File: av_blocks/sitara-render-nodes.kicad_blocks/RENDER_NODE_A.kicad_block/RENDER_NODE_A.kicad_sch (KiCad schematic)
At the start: 4 parts

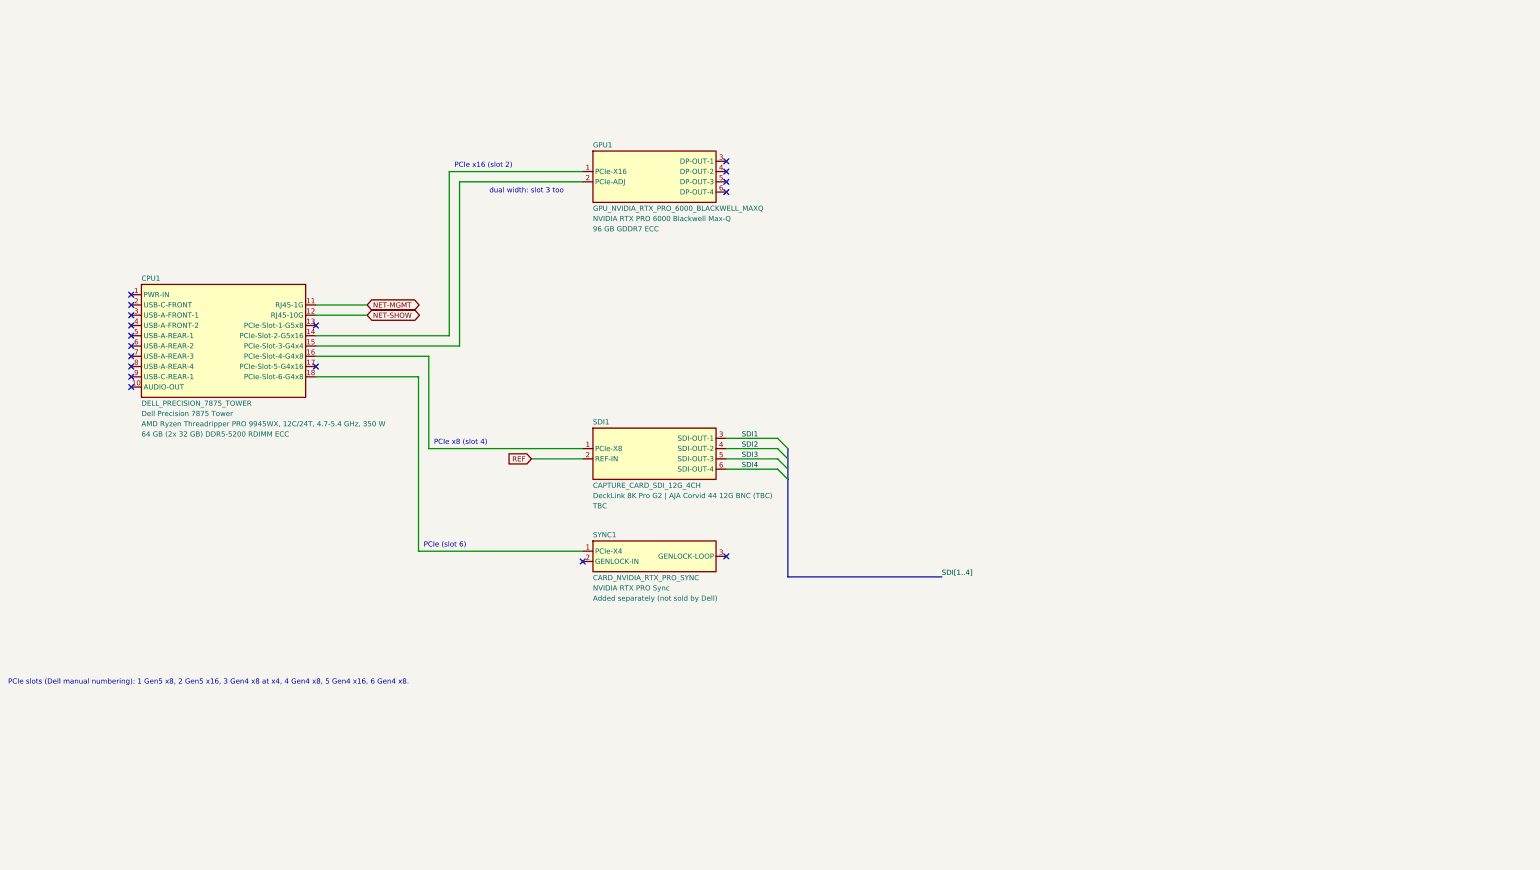
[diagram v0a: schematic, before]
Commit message: Add sitara_av generator package, project scaffolder and template, design blocks, print variant, CI and leak scan; migrate legacy pin names; add generic AV symbols and sitara-audio library
Co-Authored-By: Claude Sonnet 5.5 <noreply@anthropic.com>
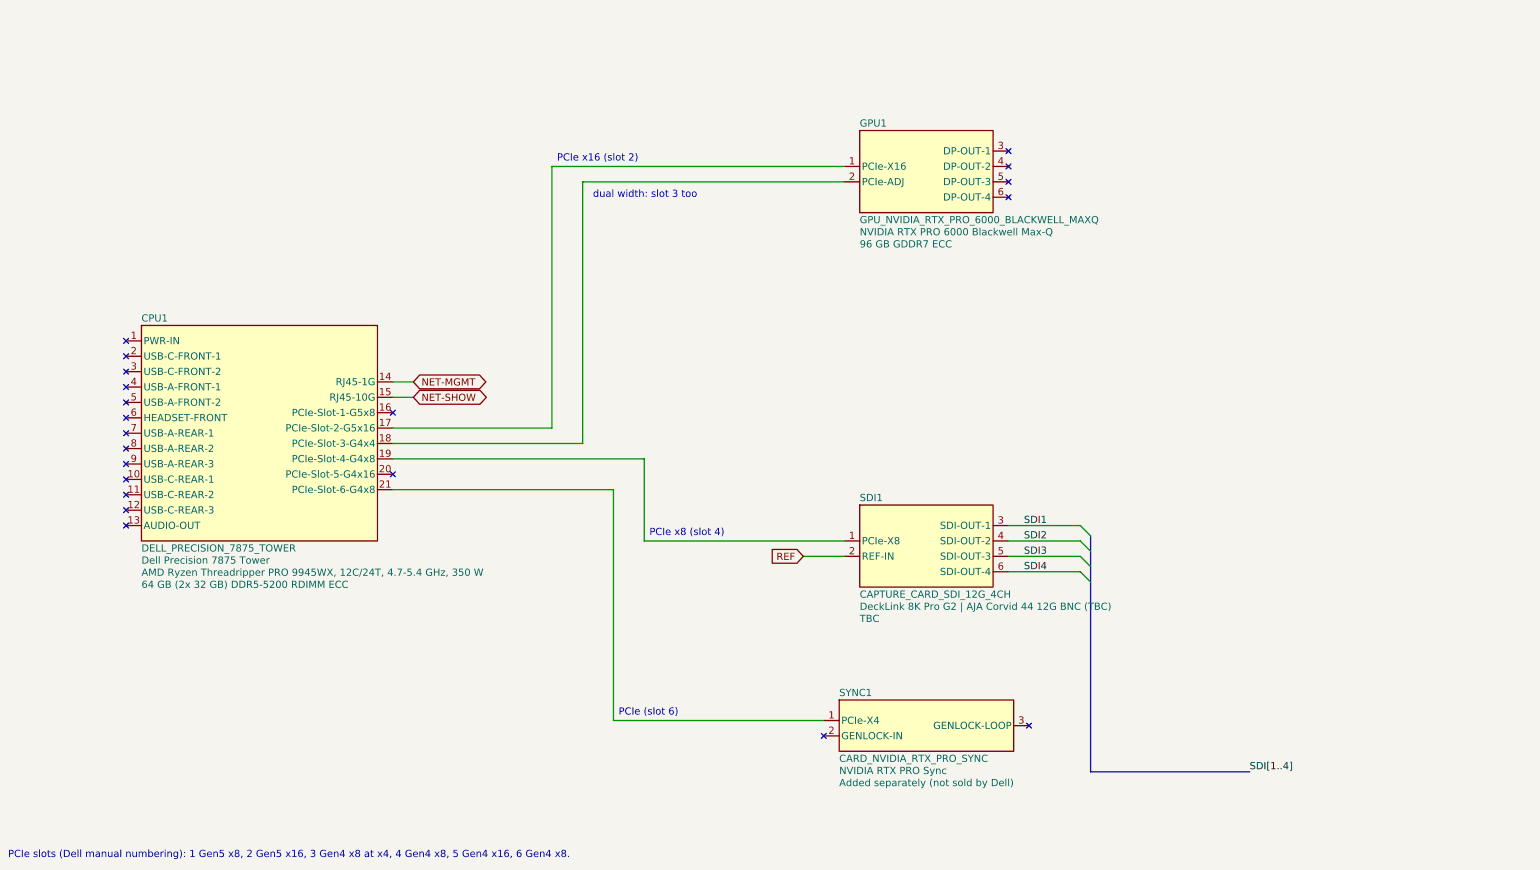
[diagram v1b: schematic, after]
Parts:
- CPU1: Ethernet RJ45 1 GbE (Realtek RTL8111-EPP) + RJ45 10 GbE (Marvell AQC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 -> (none); Management AMD DASH per Dell product page; which port carries it TBC -> AMD DASH; which port carries it TBC; Network Integrated: 1x RJ45 1 GbE + 1x RJ45 10 GbE (Dell spec page) -> Integrated: RJ45 1 GbE (Realtek RTL8111-EPP) + RJ45 10 GbE 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
- GPU1: DisplayOutputs 4x DisplayPort (DP 2.1 per NVIDIA - verify) -> 4x DisplayPort 2.1
- SYNC1: Status CONFIRMED -> TBC
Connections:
- net NET-MGMT: now also CPU1.14 (RJ45-1G); no longer CPU1.11 (RJ45-1G)
- net NET-SHOW: now also CPU1.15 (RJ45-10G); no longer CPU1.12 (RJ45-10G)
- net at CPU1.16 (PCIe-Slot-1-G5x8): no longer SDI1.1 (PCIe-X8)
- net at CPU1.18 (PCIe-Slot-3-G4x4): now also GPU1.2 (PCIe-ADJ); no longer SYNC1.1 (PCIe-X4)
- net at GPU1.1 (PCIe-X16): now also CPU1.17 (PCIe-Slot-2-G5x16); no longer CPU1.14 (PCIe-Slot-2-G5x16)
- new net: CPU1.19 (PCIe-Slot-4-G4x8), SDI1.1 (PCIe-X8)
- new net: CPU1.21 (PCIe-Slot-6-G4x8), SYNC1.1 (PCIe-X4)
- no-connect marks 18 -> 21
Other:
- title: Render node A (design block) -> Render Node A (design block)

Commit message: Add TBC register (sitara_av.tbc, av-tbc-register skill, scaffold and template page); larger note text; update Dell, Sync card and Protectli fields
Co-Authored-By: Claude Sonnet 5.5 <noreply@anthropic.com>
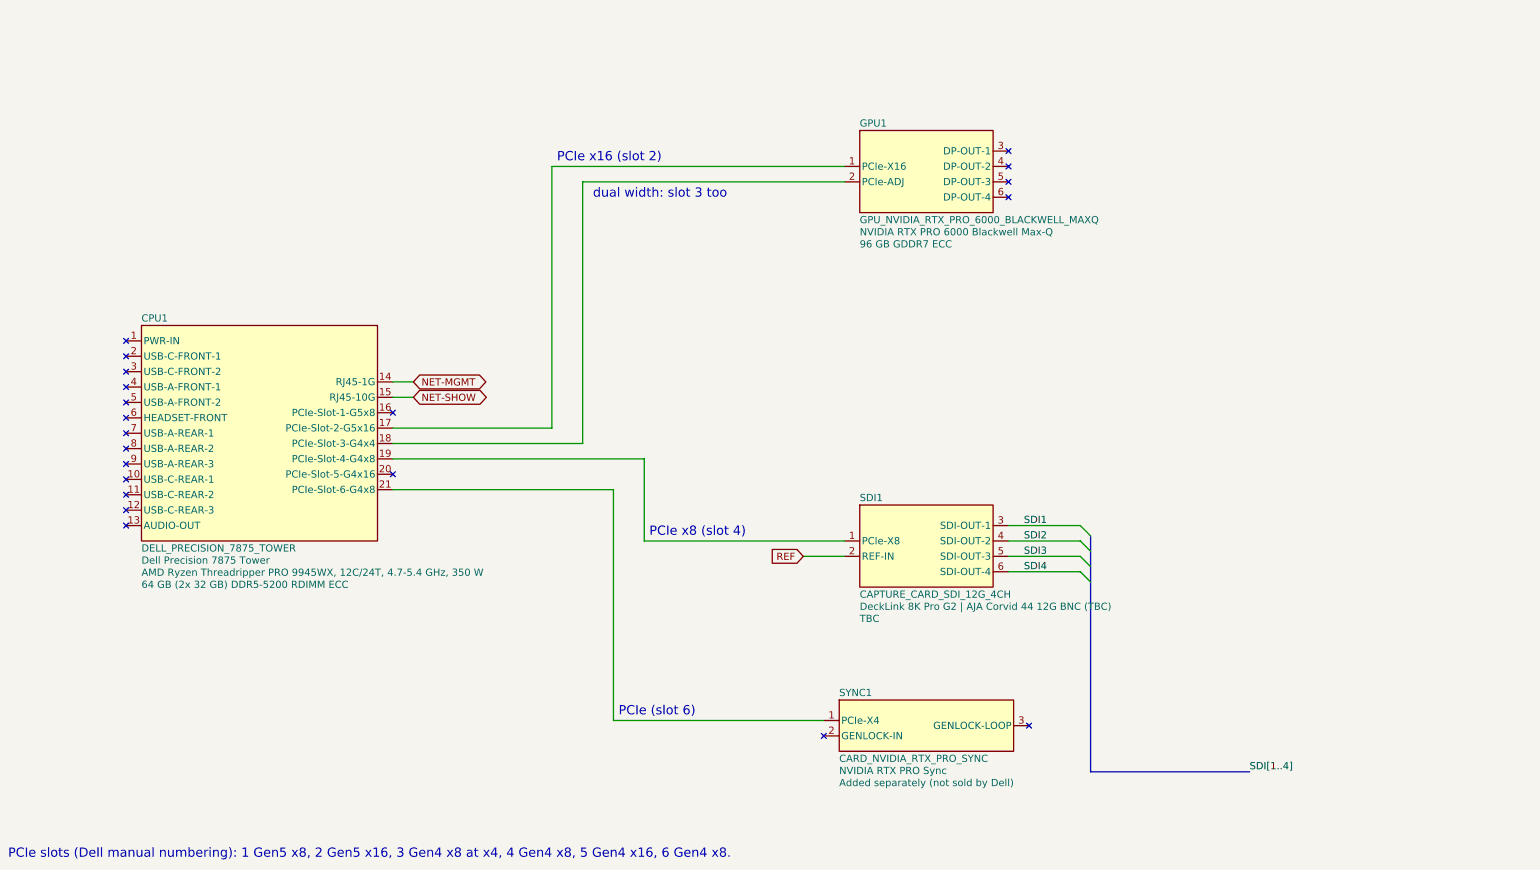
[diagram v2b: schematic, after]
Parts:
- CPU1: Management AMD DASH; which port carries it TBC -> AMD DASH; suspected on the 1 GbE jack, to be confirmed when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; Mounting (none) -> Dell rail kit 3WF88 / 03W88, 4U
- SYNC1: Lanes x4 assumed (TBC) -> Drawn as x4 for slot accounting. Reportedly uses no PCIe da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; SlotWidth 1 (assumed, TBC) -> 1 (retailer listing; vendor datasheet not found)
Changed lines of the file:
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@@
 		(effects
 			(font
-				(size 1.78 1.78)
+				(size 2.29 2.29)
 			)
 			(justify left bottom)
@@
 		(effects
 			(font
-				(size 1.78 1.78)
+				(size 2.29 2.29)
 			)
 			(justify left bottom)
@@
 		(effects
 			(font
-				(size 1.78 1.78)
+				(size 2.29 2.29)
 			)
 			(justify left bottom)
@@
 		(effects
 			(font
-				(size 1.78 1.78)
+				(size 2.29 2.29)
 			)
 			(justify left bottom)
@@
 		(effects
 			(font
-				(size 1.78 1.78)
+				(size 2.29 2.29)
 			)
 			(justify left bottom)
@@
 			)
 		)
-		(property "Management" "AMD DASH; which port carries it TBC"
+		(property "Management" "AMD DASH; suspected on the 1 GbE jack, to be confirmed when the unit arrives (Oct 28)"
 			(at 85.09 134.62 0)
 			(hide yes)
@@
 		)
 		(property "FormFactor" "Tower Workstation"
+			(at 85.09 134.62 0)
+			(hide yes)
+			(show_name no)
+			(do_not_autoplace no)
+			(effects
+				(font
+					(size 1.78 1.78)
+				)
+			)
+		)
+		(property "Mounting" "Dell rail kit 3WF88 / 03W88, 4U"
 			(at 85.09 134.62 0)
 			(hide yes)
@@
 			)
 		)
-		(property "SlotWidth" "1 (assumed, TBC)"
+		(property "SlotWidth" "1 (retailer listing; vendor datasheet not found)"
 			(at 250.19 207.01 0)
 			(hide yes)
@@
 			)
 		)
-		(property "Lanes" "x4 assumed (TBC)"
+		(property "Lanes" "Drawn as x4 for slot accounting. Reportedly uses no PCIe data lines (sync runs over ribbon cables to each GPU), electrical lanes not published"
 			(at 250.19 207.01 0)
 			(hide yes)

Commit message: Add power budget helper and PowerW symbol fields; record Dell 7875 C20 inlet and 1350 W maximum
Co-Authored-By: Claude Sonnet 5.5 <noreply@anthropic.com>
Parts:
- CPU1: PSU 1350 W -> 1350 W Platinum, C20 inlet (owner's manual); 90-264 VAC, 16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; PowerBasis (none) -> Dell PSU rating: maximum for the whole node, installed card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; PowerTypicalBasis (none) -> estimate: CPU 350 W + GPU 300 W + about 150 W other; PowerTypicalW (none) -> 800; PowerW (none) -> 1350
- GPU1: PowerBasis (none) -> NVIDIA spec (Max-Q); PowerDraw 300 W -> (none); PowerIncludedIn (none) -> host; PowerW (none) -> 300
- SDI1, SYNC1: PowerIncludedIn (none) -> host
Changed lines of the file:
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@@
 			)
 		)
-		(property "PSU" "1350 W"
+		(property "PSU" "1350 W Platinum, C20 inlet (owner's manual); 90-264 VAC, 16 A max"
+			(at 85.09 134.62 0)
+			(hide yes)
+			(show_name no)
+			(do_not_autoplace no)
+			(effects
+				(font
+					(size 1.78 1.78)
+				)
+			)
+		)
+		(property "PowerW" "1350"
+			(at 85.09 134.62 0)
+			(hide yes)
+			(show_name no)
+			(do_not_autoplace no)
+			(effects
+				(font
+					(size 1.78 1.78)
+				)
+			)
+		)
+		(property "PowerBasis" "Dell PSU rating: maximum for the whole node, installed cards included"
+			(at 85.09 134.62 0)
+			(hide yes)
+			(show_name no)
+			(do_not_autoplace no)
+			(effects
+				(font
+					(size 1.78 1.78)
+				)
+			)
+		)
+		(property "PowerTypicalW" "800"
+			(at 85.09 134.62 0)
+			(hide yes)
+			(show_name no)
+			(do_not_autoplace no)
+			(effects
+				(font
+					(size 1.78 1.78)
+				)
+			)
+		)
+		(property "PowerTypicalBasis" "estimate: CPU 350 W + GPU 300 W + about 150 W other"
 			(at 85.09 134.62 0)
 			(hide yes)
@@
 			)
 		)
+		(property "PowerIncludedIn" "host"
+			(at 250.19 207.01 0)
+			(hide yes)
+			(show_name no)
+			(do_not_autoplace no)
+			(effects
+				(font
+					(size 1.78 1.78)
+				)
+			)
+		)
 		(property "Model" "NVIDIA RTX PRO Sync"
 			(at 228.6 217.12 0)
@@
 			)
 		)
-		(property "PowerDraw" "300 W"
+		(property "PowerW" "300"
+			(at 250.19 69.85 0)
+			(hide yes)
+			(show_name no)
+			(do_not_autoplace no)
+			(effects
+				(font
+					(size 1.78 1.78)
+				)
+			)
+		)
+		(property "PowerBasis" "NVIDIA spec (Max-Q)"
+			(at 250.19 69.85 0)
+			(hide yes)
+			(show_name no)
+			(do_not_autoplace no)
+			(effects
+				(font
+					(size 1.78 1.78)
+				)
+			)
+		)
+		(property "PowerIncludedIn" "host"
 			(at 250.19 69.85 0)
 			(hide yes)
@@
 			(at 250.19 162.56 0)
 			(hide yes)
+			(show_name no)
+			(do_not_autoplace no)
+			(effects
+				(font
+					(size 1.78 1.78)
+				)
+			)
+		)
+		(property "PowerIncludedIn" "host"
+			(at 250.19 162.56 0)
+			(hide yes)

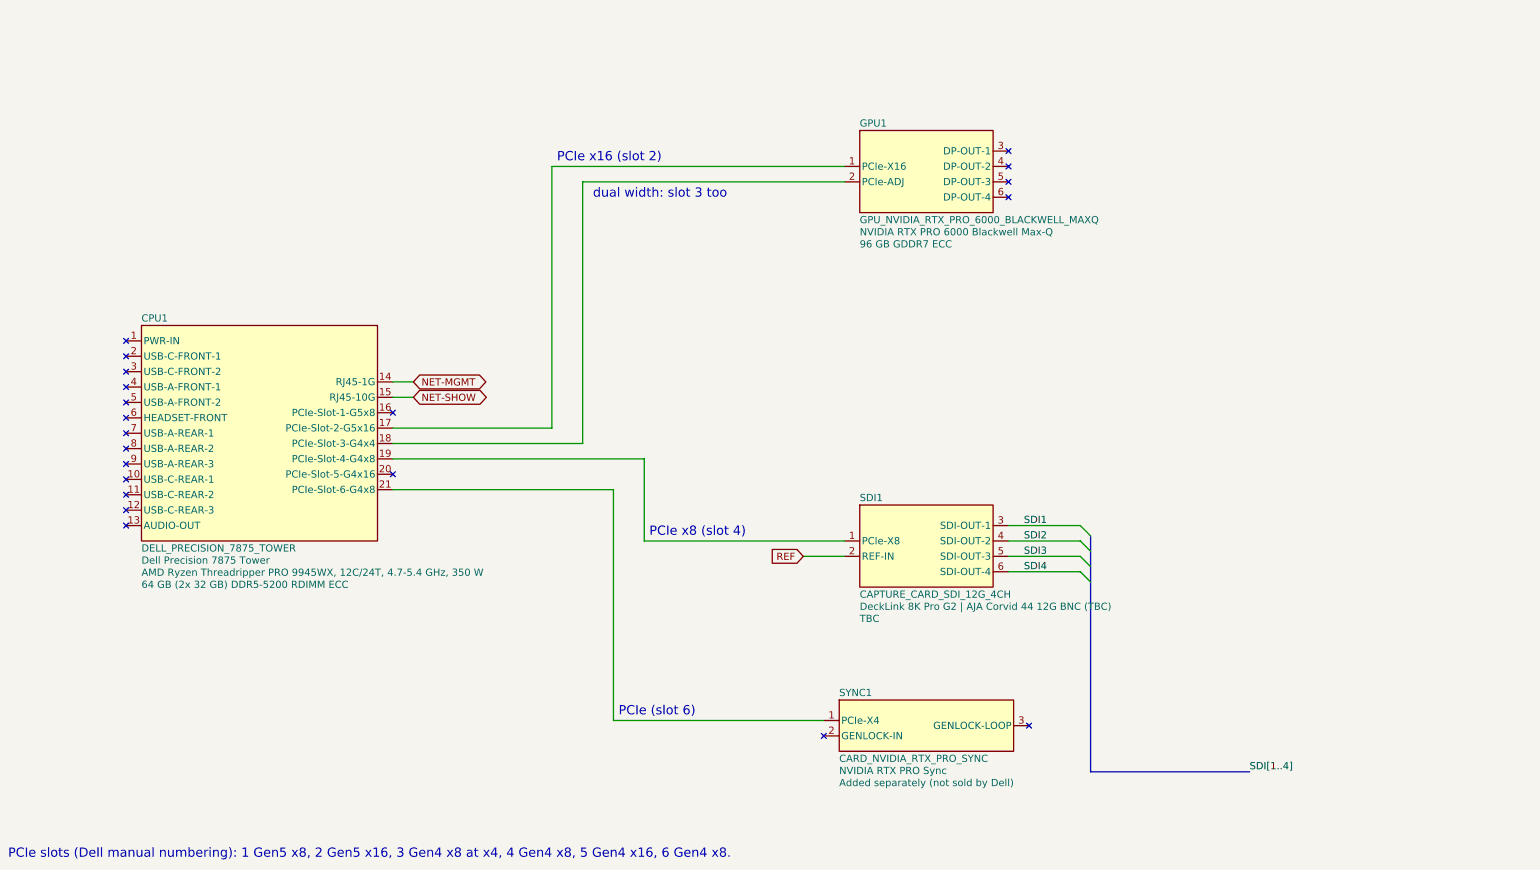
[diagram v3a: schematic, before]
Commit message: Render node block: Sync in slot 1, SDI card in slot 5, slots 4 and 6 empty; TBC register supports 16 rows
Co-Authored-By: Claude Sonnet 5.5 <noreply@anthropic.com>
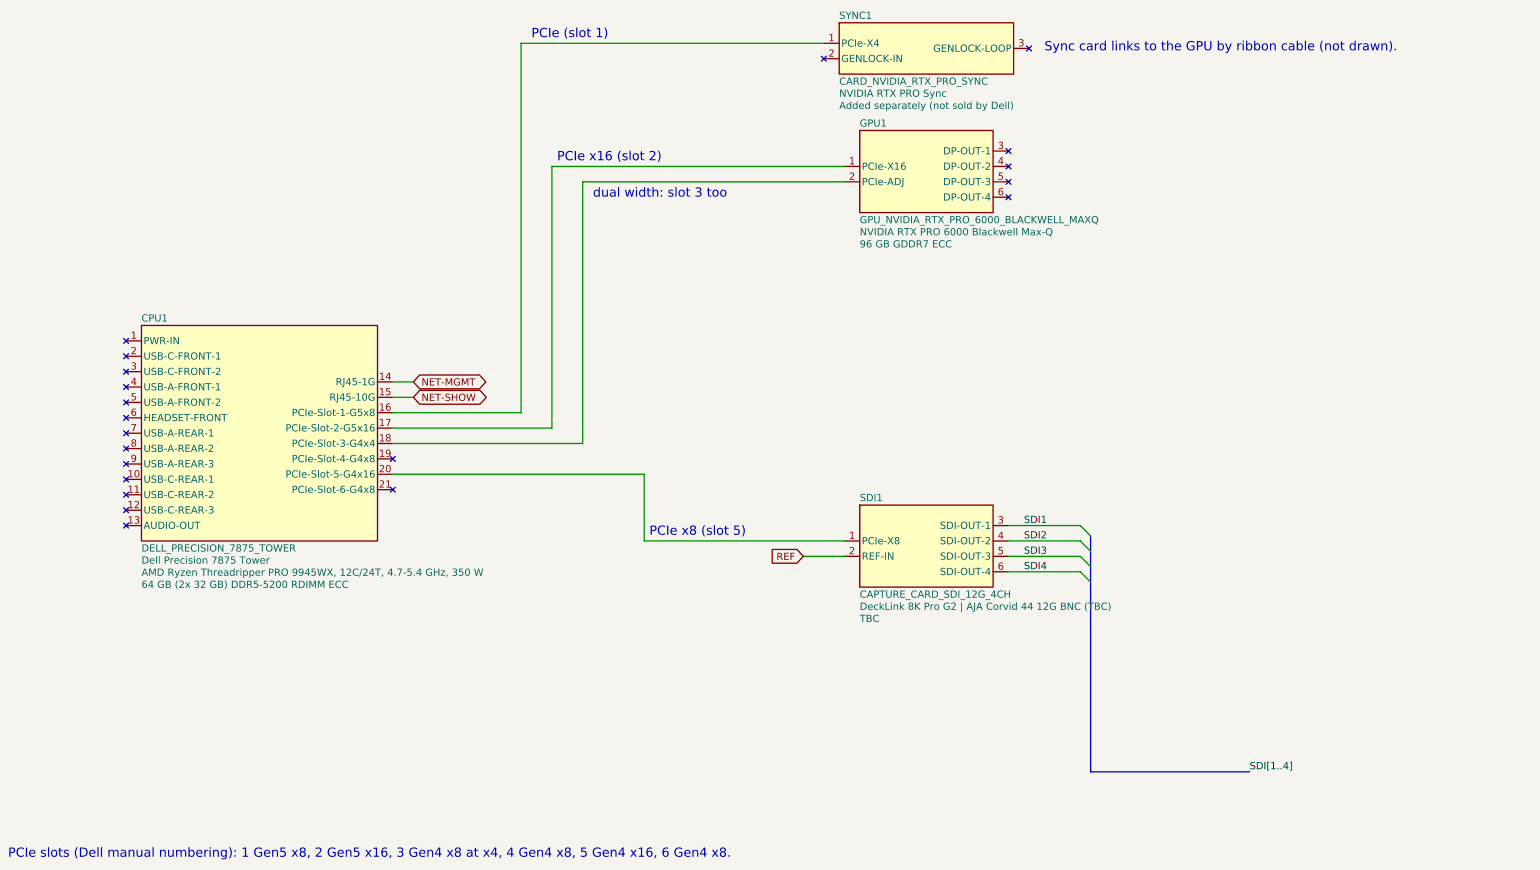
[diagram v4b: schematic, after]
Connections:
- net at CPU1.16 (PCIe-Slot-1-G5x8): now also SYNC1.1 (PCIe-X4)
- net at CPU1.19 (PCIe-Slot-4-G4x8): no longer SDI1.1 (PCIe-X8)
- net at CPU1.20 (PCIe-Slot-5-G4x16): now also SDI1.1 (PCIe-X8)
- net at CPU1.21 (PCIe-Slot-6-G4x8): no longer SYNC1.1 (PCIe-X4)
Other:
- note added: "PCIe (slot 1)"
- note added: "PCIe x8 (slot 5)"
- note added: "Sync card links to the GPU by ribbon cable (not drawn)."
- note removed: "PCIe (slot 6)"
- note removed: "PCIe x8 (slot 4)"
- moved on the sheet: SYNC1
